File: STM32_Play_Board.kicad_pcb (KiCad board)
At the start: 2 copper layers, 95 parts, among them J1 USB_B_Micro, J10 Conn_01x30_Pin, J11 Conn_01x03_Pin, J12 Conn_01x03_Pin, J13 Conn_01x03_Pin, J14 Conn_01x03_Pin, J2 Micro_SD_Card, J3 Conn_01x02_Socket, J4 Conn_01x01_Pin, J5 Conn_01x01_Pin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

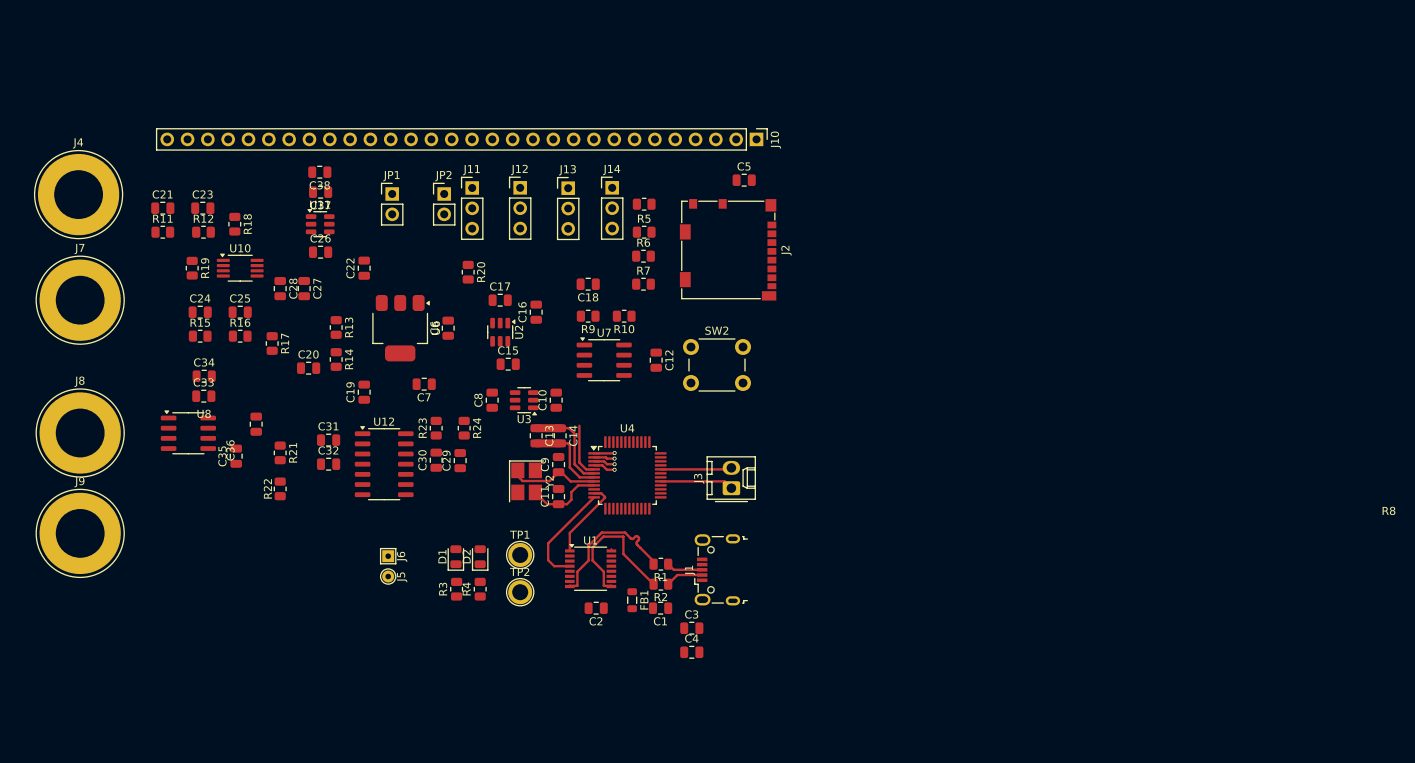
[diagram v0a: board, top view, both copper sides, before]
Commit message: changed schematics
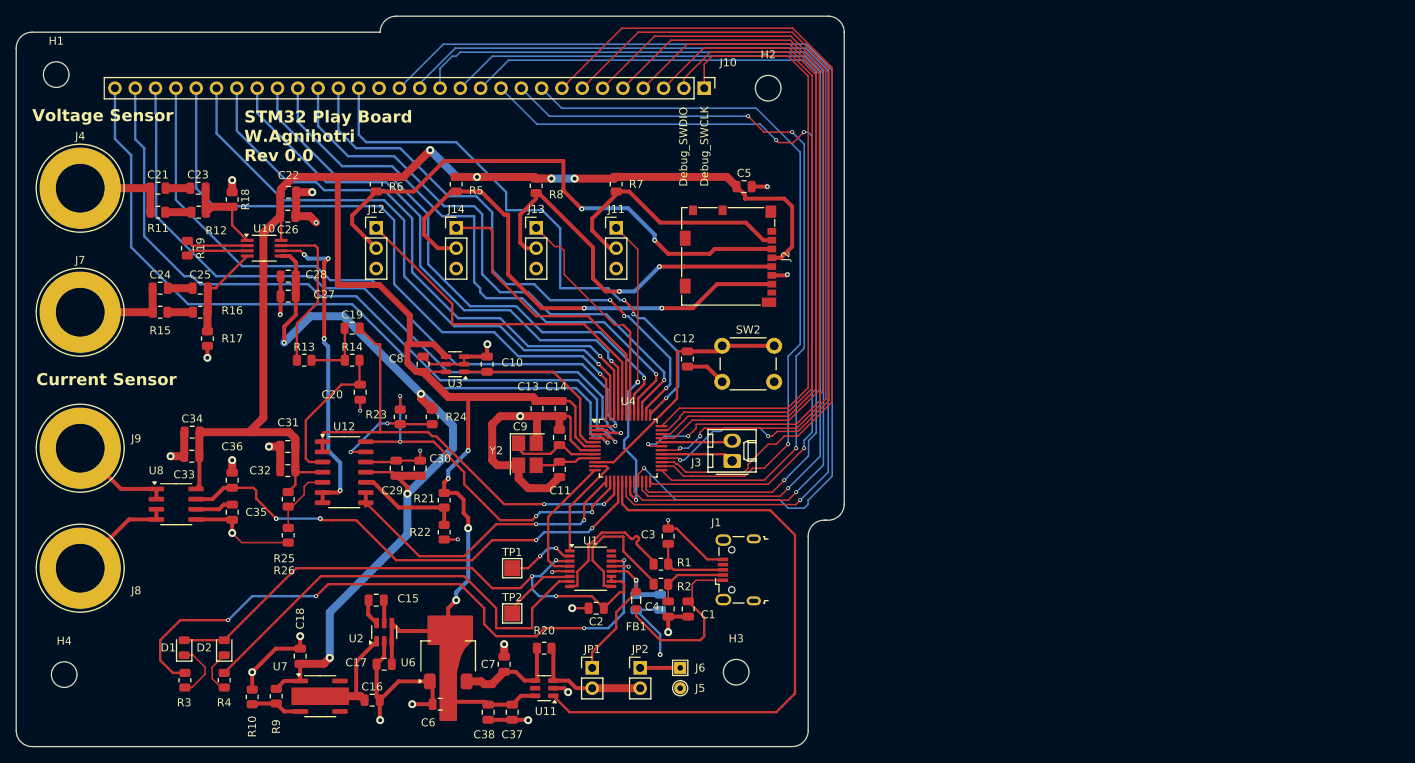
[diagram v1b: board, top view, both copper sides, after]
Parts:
- added C39: 4.7 uF, Capacitor_SMD:C_0805_2012Metric, B.Cu at (162.5, 114.3)
- added C40: 100 nF, Capacitor_SMD:C_0805_2012Metric, B.Cu at (165.5, 114.2)
- added G***: LOGO, LOGO, B.Cu at (132.4, 94.7)
- added H1: MountingHole, MountingHole:MountingHole_3.2mm_M3, F.Cu at (90.0, 48.3)
- added H2: MountingHole, MountingHole:MountingHole_3.2mm_M3, F.Cu at (179.0, 50.0)
- added H3: MountingHole, MountingHole:MountingHole_3.2mm_M3, F.Cu at (175.0, 123.0)
- added H4: MountingHole, MountingHole:MountingHole_3.2mm_M3, F.Cu at (91.0, 123.3)
- added R25: 10.6k, Resistor_SMD:R_0805_2012Metric, F.Cu at (119.0, 101.4)
- added R26: 10k, Resistor_SMD:R_0805_2012Metric, F.Cu at (119.0, 105.9)
- C1: value 4.7 pF -> 10 nF
- C10: value 4.7 uF -> 1 nF
- C18: value 10 uF -> 1 uF
- C8: value 4.7 uF -> 2 uF
- R11, R12, R15, R16: value 500 -> 1M
- R17, R18: value 200 -> 10k
- R19: value 16k -> 84.5k
- R3, R4: value 470 -> 750
- TP1, TP2: footprint TestPoint:TestPoint_Plated_Hole_D2.0mm -> TestPoint:TestPoint_Pad_2.0x2.0mm
- moved C38 70.7 mm to (144.0, 128.0), turned to -90 degrees
- moved C37 69.3 mm to (147.0, 128.0), turned to -90 degrees
- moved R10 66.5 mm to (114.5, 126.1), turned to -90 degrees
- moved U11 64.4 mm to (151.0, 125.0), turned to 180 degrees
- moved JP1 64.3 mm to (157.0, 122.5)
- moved JP2 64.1 mm to (163.0, 122.5)
- moved R9 61.5 mm to (117.5, 126.0), turned to 90 degrees
- moved C18 58.8 mm to (120.5, 121.0), turned to -90 degrees
- moved U7 55.0 mm to (123.0, 126.0)
- moved C16 52.7 mm to (129.5, 126.5), turned to 0 degrees
- moved R20 48.0 mm to (151.0, 120.0), turned to 180 degrees
- moved C17 47.8 mm to (131.0, 122.0), turned to 180 degrees
- moved C6 47.0 mm to (138.0, 127.0), turned to 180 degrees
- moved U6 41.4 mm to (139.0, 121.0), turned to 90 degrees
- moved U2 40.2 mm to (131.0, 118.0), turned to 90 degrees
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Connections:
- C27 pad 1: -3V3 -> Earth
- C27 pad 2: Earth -> -3V3
- C28 pad 1: -3V3 -> Earth
- C28 pad 2: Earth -> -3V3
- C36 pad 2: Net-(U12B-+) -> /Micrcontroller STM32C0/Curr_meas
- J10 pad 1: /Connectors/PB6 -> /Connectors/DEBUG_SWCLK
- J10 pad 10: /Connectors/PB15 -> /Connectors/PB14
- J10 pad 11: /Connectors/PA11/PA9 -> /Connectors/PB12
- J10 pad 12: /Connectors/PA12/PA10 -> /Connectors/PB11
- J10 pad 13: /Connectors/PA13 -> /Connectors/PB10
- J10 pad 14: /Connectors/PA14 -> /Connectors/PB1
- J10 pad 16: /Connectors/PF3 -> /Connectors/PB2
- J10 pad 17: /Connectors/PD0 -> unconnected-(J10-Pin_17-Pad17)
- J10 pad 18: /Connectors/PD1 -> /Micrcontroller STM32C0/UART2_Rx
- J10 pad 19: /Connectors/PD2 -> /Connectors/PD0
- J10 pad 2: /Connectors/PB7 -> /Connectors/DEBUG_SWDIO
- J10 pad 20: /Connectors/PD3 -> /Connectors/PD1
- J10 pad 21: /Connectors/PC6 -> /Connectors/PD2
- J10 pad 22: /Connectors/PC7 -> /Connectors/PD3
- J10 pad 23: /Connectors/PC13 -> /Connectors/PB6
- J10 pad 24: /Connectors/PC14 -> /Connectors/PB7
- J10 pad 25: /Connectors/PC15 -> /Connectors/PB8
- J10 pad 26: /Connectors/PB1 -> /Connectors/PB9
- J10 pad 27: /Connectors/PB2 -> /Connectors/PC13
- J10 pad 28: /Micrcontroller STM32C0/UART2_Tx -> /Connectors/PC14
- J10 pad 29: /Micrcontroller STM32C0/UART2_Rx -> /Connectors/PC15
- J10 pad 3: /Connectors/PB8 -> /Connectors/PA12/PA10
- J10 pad 30: unconnected-(J10-Pin_30-Pad30) -> /Connectors/PF3
- J10 pad 4: /Connectors/PB9 -> /Connectors/PA11/PA9
- J10 pad 5: /Connectors/PB10 -> /Connectors/PC7
- J10 pad 6: /Connectors/PB11 -> /Connectors/PC6
- J10 pad 7: /Connectors/PB12 -> /Micrcontroller STM32C0/UART2_Tx
- J10 pad 8: /Connectors/PB13 -> /Connectors/PB15
- J10 pad 9: /Connectors/PB14 -> /Connectors/PB13
- J11 pad 1: /SD_CARD/SPI_Cs_SD -> /Micrcontroller STM32C0/SPI_Cs
- J11 pad 2: /Micrcontroller STM32C0/SPI_Cs -> /SD_CARD/SPI_Cs_SD
- J12 pad 1: /SD_CARD/SPI_Mosi_SD -> /Micrcontroller STM32C0/SPI_Mosi
- J12 pad 2: /Micrcontroller STM32C0/SPI_Mosi -> /SD_CARD/SPI_Mosi_SD
- J13 pad 1: /SD_CARD/SPI_Clk_SD -> /Micrcontroller STM32C0/SPI_Clk
- J13 pad 2: /Micrcontroller STM32C0/SPI_Clk -> /SD_CARD/SPI_Clk_SD
- J14 pad 1: /SD_CARD/SPI_Miso_SD -> /Micrcontroller STM32C0/SPI_Miso
- J14 pad 2: /Micrcontroller STM32C0/SPI_Miso -> /SD_CARD/SPI_Miso_SD
- U10 pad 6: Earth -> /Voltage and Current Measurement/1.6 V Ref
- U12 pad 6: /Micrcontroller STM32C0/Curr_meas -> /Voltage and Current Measurement/1.6 V Ref
- U12 pad 7: /Micrcontroller STM32C0/Curr_meas -> /Voltage and Current Measurement/1.6 V Ref
- U4 pad 35: /Connectors/PA13 -> /Connectors/DEBUG_SWDIO
- U4 pad 36: /Connectors/PA14 -> /Connectors/DEBUG_SWCLK
- U8 pad 7: Net-(U12B-+) -> /Micrcontroller STM32C0/Curr_meas
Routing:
- net +3.3V: track 11.8 -> 280.0 mm, vias 0 -> 8
- net Earth: track 10.6 -> 182.2 mm, vias 0 -> 29
- net /Connectors/PB2: track 0.00 -> 138.0 mm, vias 0 -> 1
- net /Connectors/PA7: track 0.00 -> 134.0 mm, vias 0 -> 1
- net /Connectors/PB1: track 0.00 -> 128.7 mm, vias 0 -> 1
- net /Connectors/PB10: track 0.00 -> 121.2 mm, vias 0 -> 1
- net /Connectors/PB11: track 0.00 -> 115.7 mm, vias 0 -> 1
- net /Connectors/PB15: track 0.00 -> 106.5 mm
- net /Connectors/PB12: track 0.00 -> 103.1 mm, vias 0 -> 3
- net /Micrcontroller STM32C0/UART2_Tx: track 0.00 -> 102.0 mm, vias 0 -> 2
- net -3V3: track 0.00 -> 98.8 mm, vias 0 -> 4
- net /Connectors/PC6: track 0.00 -> 96.9 mm, vias 0 -> 2
- net /Connectors/PC7: track 0.00 -> 96.0 mm, vias 0 -> 2
- net /Connectors/PB14: track 0.00 -> 95.7 mm, vias 0 -> 3
- net /Connectors/PF3: track 2.79 -> 94.5 mm
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- added copper zone on In1.Cu, net Earth
- added copper zone on In2.Cu, net Earth
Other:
- board outline added: 103.5 x 91.3 mm
- copper layers 2 -> 4
- board text added: "Current Sensor"
- board text added: "Debug_SWCLK"
- board text added: "Debug_SWDIO"
- board text added: "STM32 Play Board W.Agnihotri Rev 0.0"
- board text added: "Voltage Sensor"
